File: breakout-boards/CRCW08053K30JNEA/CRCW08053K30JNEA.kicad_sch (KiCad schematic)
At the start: 0 parts

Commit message: feat: add 3.3k ohm resistor breakout board
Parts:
- added J1, J2: Conn_01x12, Connector_PinSocket_2.54mm:PinSocket_1x12_P2.54mm_Vertical, symbol Connector_Generic:Conn_01x12
- added R1, R10, R11, R12, R2, R3, R4, R5, R6, R7, R8, R9: 3K3Ω, RESC2012X50N, symbol FixedWing:CRCW08053K30JNEA
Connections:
- new net: J1.7 (Pin_7), R6.1
- new net: J2.7 (Pin_7), R6.2
- new net: J1.8 (Pin_8), R5.1
- new net: J2.8 (Pin_8), R5.2
- new net: J1.4 (Pin_4), R9.1
- new net: J2.4 (Pin_4), R9.2
- new net: J1.1 (Pin_1), R12.1
- new net: J1.10 (Pin_10), R3.1
- new net: J1.11 (Pin_11), R2.1
- new net: J1.12 (Pin_12), R1.1
- new net: J1.2 (Pin_2), R11.1
- new net: J1.3 (Pin_3), R10.1
- new net: J1.5 (Pin_5), R8.1
- new net: J1.6 (Pin_6), R7.1
- new net: J1.9 (Pin_9), R4.1
- new net: J2.9 (Pin_9), R4.2
- new net: J2.2 (Pin_2), R11.2
- new net: J2.3 (Pin_3), R10.2
- new net: J2.1 (Pin_1), R12.2
- new net: J2.10 (Pin_10), R3.2
- new net: J2.11 (Pin_11), R2.2
- new net: J2.12 (Pin_12), R1.2
- new net: J2.5 (Pin_5), R8.2
- new net: J2.6 (Pin_6), R7.2

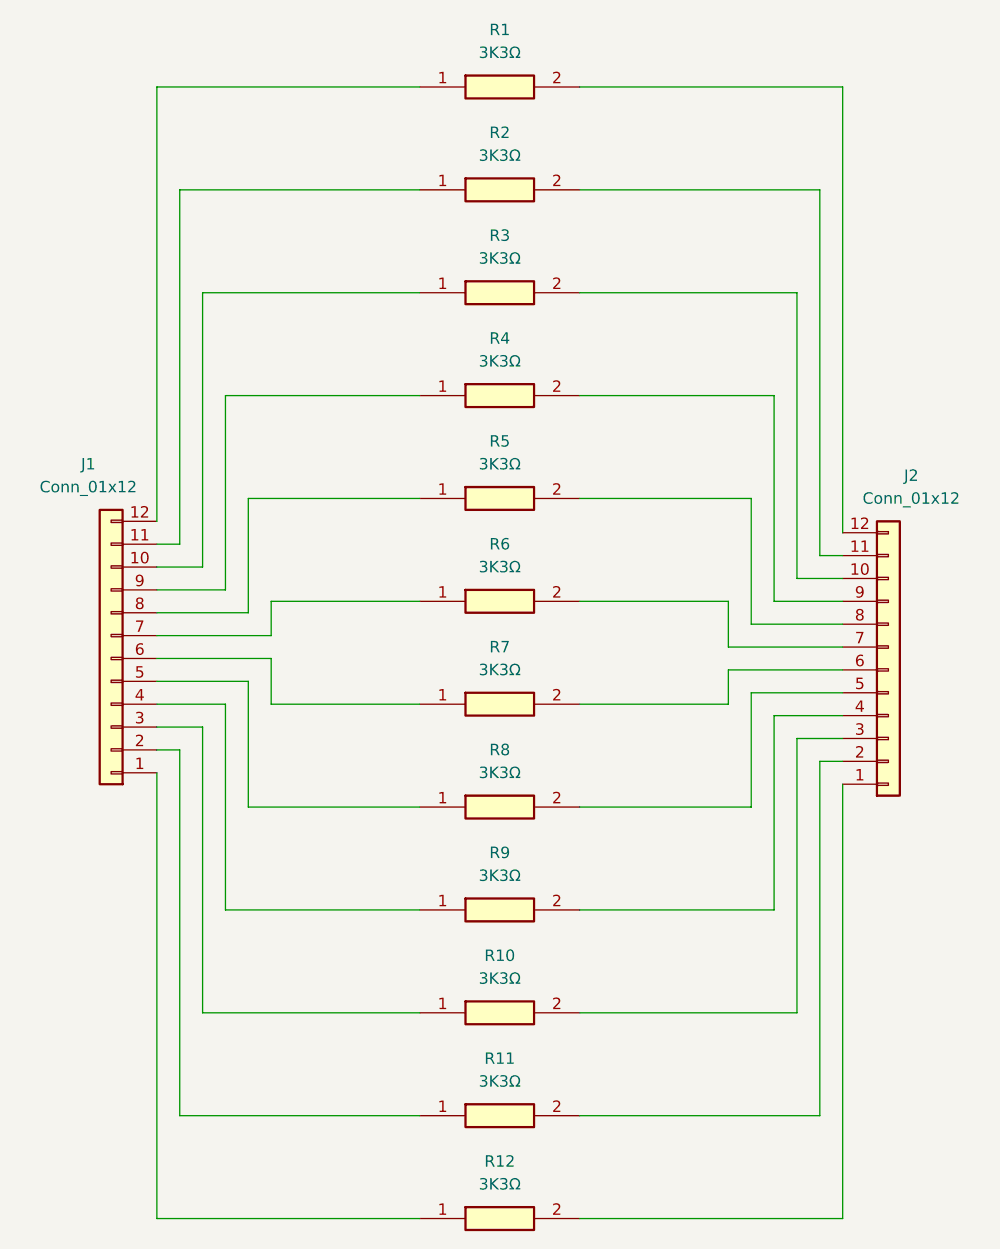
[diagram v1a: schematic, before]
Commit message: feat: create footprints for resistor breakout boards
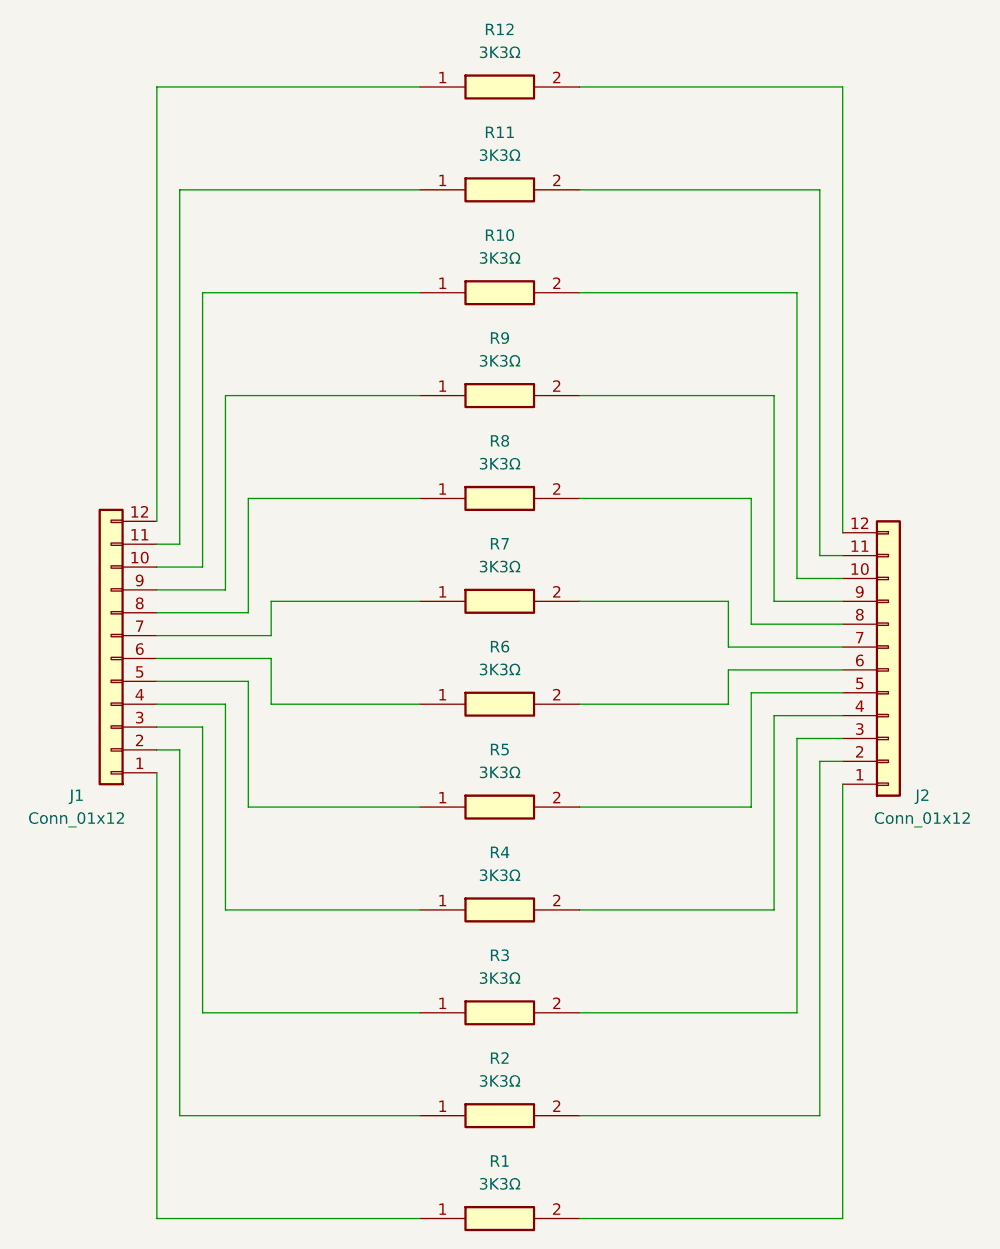
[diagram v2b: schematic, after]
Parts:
- renumbered R12 to R1, R3 to R10, R2 to R11, R1 to R12, R11 to R2, R10 to R3, R9 to R4, R8 to R5, R7 to R6, R6 to R7, R5 to R8, R4 to R9
